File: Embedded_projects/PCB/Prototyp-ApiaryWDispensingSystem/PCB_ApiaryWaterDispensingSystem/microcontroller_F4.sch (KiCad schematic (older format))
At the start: 77 parts, among them J10 Conn_02x19_Odd_Even, J7 Conn_02x19_Odd_Even, SW1 SW_Push_Dual, Y2 Crystal_GND23_Small, Y3 Crystal

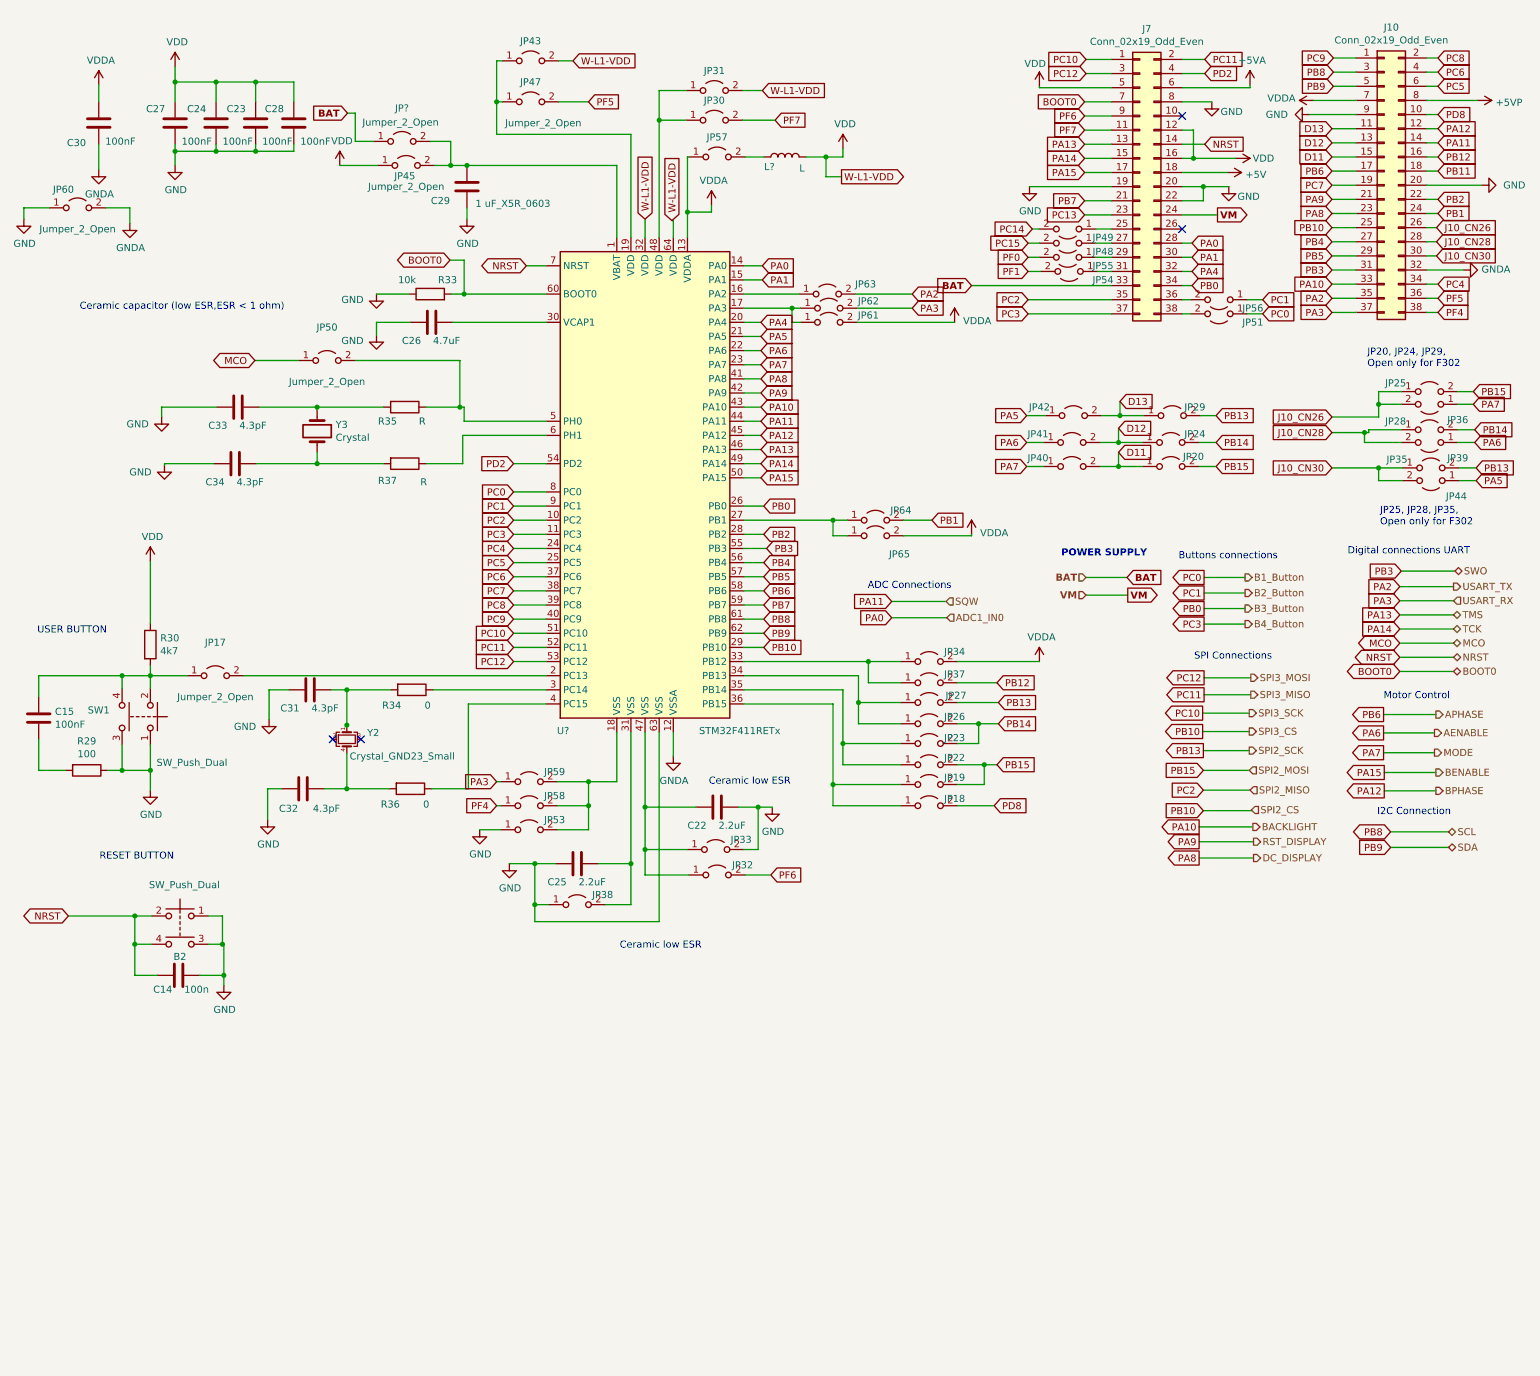
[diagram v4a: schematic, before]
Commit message: All signal has been routed, the analog part needs to be completed
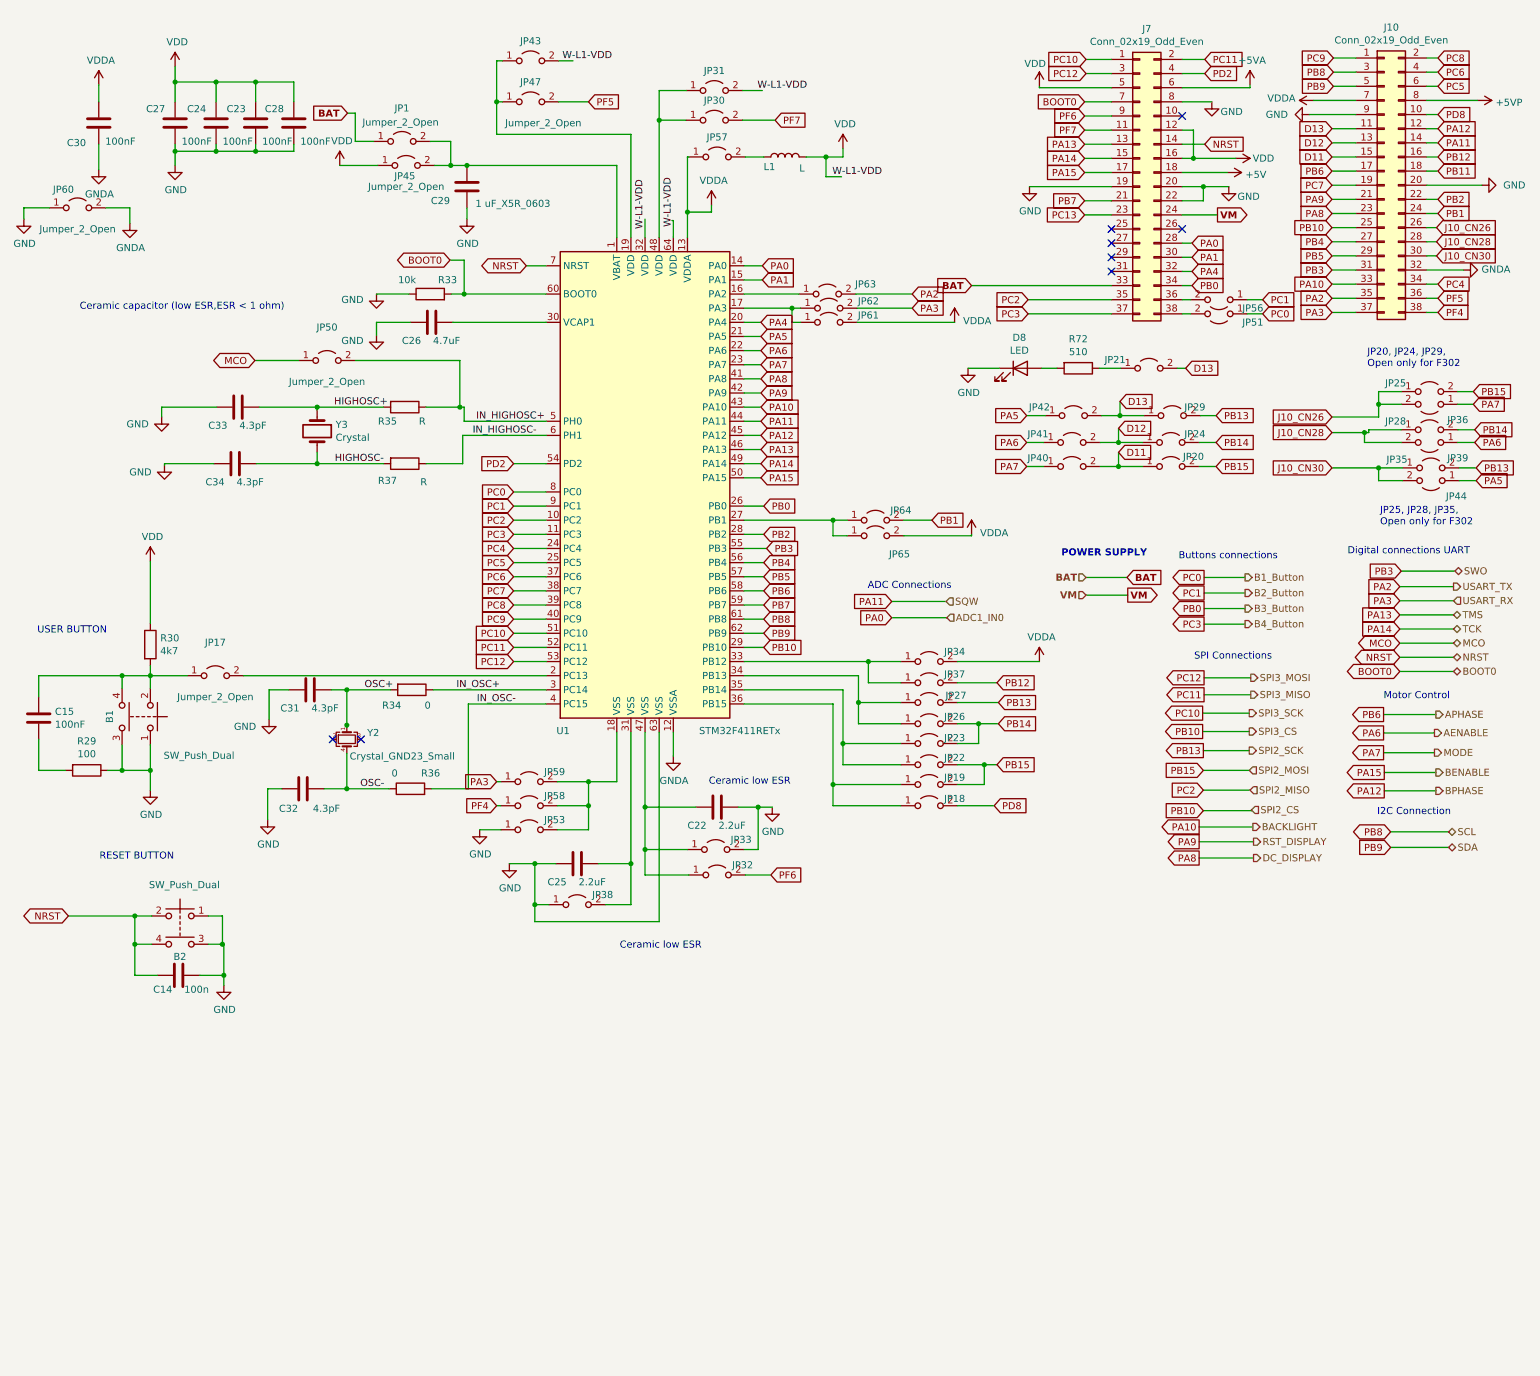
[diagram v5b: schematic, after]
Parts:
- removed JP48, JP49, JP54, JP55: Jumper_2_Open, Jumper:SolderJumper-2_P1.3mm_Open_TrianglePad1.0x1.5mm, symbol Jumper:Jumper_2_Open
- removed SW1: SW_Push_Dual, Button_Switch_SMD:SW_Push_1P1T_NO_6x6mm_H9.5mm, symbol Switch:SW_Push_Dual
- added B1: SW_Push_Dual, Button_Switch_SMD:SW_SPST_Omron_B3FS-100xP, symbol Switch:SW_Push_Dual
- added D8: LED, LED_SMD:LED_0805_2012Metric, symbol Device:LED
- added JP21: Jumper_2_Open, Jumper:SolderJumper-2_P1.3mm_Open_TrianglePad1.0x1.5mm, symbol Jumper:Jumper_2_Open
- added R72: 510, Resistor_SMD:R_0603_1608Metric, symbol Device:R
- B2: footprint Button_Switch_SMD:SW_Push_1P1T_NO_6x6mm_H9.5mm -> Button_Switch_SMD:SW_SPST_Omron_B3FS-100xP
- J10, J7: footprint (none) -> Connector_PinHeader_2.54mm:PinHeader_2x19_P2.54mm_Vertical
- gave numbers to parts that had none: 3
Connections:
- net D13: now also JP21.2 (B)
- net GND: now also B1.1, B1.3, D8.1 (K)
- net at C15.1, JP17.1 (A), R30.2: now also B1.2, B1.4
- net IN_OSC+: now reaches R34.1, U1.3 (PC14)
- net IN_OSC-: now reaches U1.4 (PC15)
- net IN_OSC-: now also R36.2; no longer R36.1
- net IN_HIGHOSC+: now reaches JP50.2 (B), R35.1, U1.5 (PH0)
- net IN_HIGHOSC-: now reaches R37.1, U1.6 (PH1)
- net OSC+: now reaches C31.1, R34.2, Y2.1
- net OSC-: now reaches C32.1, Y2.4
- net OSC-: now also R36.1; no longer R36.2
- net HIGHOSC+: now reaches C33.1, R35.2, Y3.1
- net HIGHOSC-: now reaches C34.1, R37.2, Y3.2
- new net: JP21.1 (A), R72.1
- new net: D8.2 (A), R72.2
- no-connect marks 4 -> 8
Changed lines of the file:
@@
 $EndDescr
-$Comp
-L Switch:SW_Push_Dual SW1
-U 1 1 67E57DF4
-P 1510 5450
-F 0 "SW1" V 1556 5162 50  0000 R CNN
-F 1 "SW_Push_Dual" V 1185 5995 50  0000 R CNN
-F 2 "Button_Switch_SMD:SW_Push_1P1T_NO_6x6mm_H9.5mm" H 1510 5650 50  0001 C CNN
-F 3 "~" H 1510 5650 50  0001 C CNN
-	1    1510 5450
-	0    1    -1   0
-$EndComp
 $Comp
 L Device:R R30
@@
 	1    0    0    -1
 $EndComp
-$Comp
-L MCU_ST_STM32F4:STM32F411RETx U?
-U 1 1 67E5B943
-P 5010 3760
-F 0 "U?" H 4430 1970 50  0000 C CNN
-F 1 "STM32F411RETx" H 5680 1970 50  0000 C CNN
-F 2 "Package_QFP:LQFP-64_10x10mm_P0.5mm" H 4410 2060 50  0001 R CNN
-F 3 "http://www.st.com/st-web-ui/static/active/en/resource/technical/document/datasheet/DM00115249.pdf" H 5010 3760 50  0001 C CNN
-	1    5010 3760
-	1    0    0    -1
-$EndComp
-Wire Wire Line
-	1510 5250 1510 5160
 Wire Wire Line
 	1310 5250 1310 5160
@@
 $EndComp
 Wire Wire Line
-	1510 5650 1510 5830
-Wire Wire Line
 	1310 5650 1310 5830
 Wire Wire Line
 	1310 5830 1510 5830
-Connection ~ 1510 5830
 Wire Wire Line
 	1510 5830 1510 5970
@@
 F 3 "~" H 3350 5960 50  0001 C CNN
 	1    3350 5960
-	0    1    1    0
+	0    -1   -1   0
 $EndComp
 Wire Wire Line
@@
 	3730 3260 3700 3260
 Wire Wire Line
-	3160 3260 2690 3260
-Wire Wire Line
 	2690 3260 2690 3280
 Wire Wire Line
@@
 Wire Wire Line
 	5700 1230 5930 1230
-Text GLabel 4500 810  2    50   Input ~ 0
-W-L1-VDD
-Text GLabel 5010 1930 1    50   Input ~ 0
-W-L1-VDD
 Wire Wire Line
 	4500 810  4400 810
@@
 	5310 1490 5320 1490
 $Comp
-L Device:L L?
+L Device:L L1
 U 1 1 67F1388C
 P 6000 1490
-F 0 "L?" V 5930 1600 50  0000 C CNN
+F 0 "L1" V 5930 1600 50  0000 C CNN
 F 1 "L" V 5920 1370 50  0000 C CNN
 F 2 "Inductor_SMD:L_0603_1608Metric" H 6000 1490 50  0001 C CNN
@@
 	1    0    0    -1
 $EndComp
-Text GLabel 6400 1630 2    50   Output ~ 0
-W-L1-VDD
 Wire Wire Line
 	6150 1490 6290 1490
@@
 Wire Wire Line
 	6510 2660 7200 2660
-Text GLabel 5840 1020 2    50   Input ~ 0
-W-L1-VDD
 Wire Wire Line
 	5840 1020 5700 1020
@@
 F 0 "B2" H 1766 6572 50  0000 R CNN
 F 1 "SW_Push_Dual" H 1940 7080 50  0000 R CNN
-F 2 "Button_Switch_SMD:SW_Push_1P1T_NO_6x6mm_H9.5mm" H 1720 7060 50  0001 C CNN
+F 2 "Button_Switch_SMD:SW_SPST_Omron_B3FS-100xP" H 1720 7060 50  0001 C CNN
 F 3 "~" H 1720 7060 50  0001 C CNN
 	1    1720 6860
@@
 F 0 "J7" H 8560 2817 50  0000 C CNN
 F 1 "Conn_02x19_Odd_Even" H 8560 2726 50  0000 C CNN
-F 2 "" H 8510 1700 50  0001 C CNN
+F 2 "Connector_PinHeader_2.54mm:PinHeader_2x19_P2.54mm_Vertical" H 8510 1700 50  0001 C CNN
 F 3 "~" H 8510 1700 50  0001 C CNN
 	1    8510 1700
@@
 F 0 "J10" H 10290 2807 50  0000 C CNN
 F 1 "Conn_02x19_Odd_Even" H 10290 2716 50  0000 C CNN
-F 2 "" H 10240 1690 50  0001 C CNN
+F 2 "Connector_PinHeader_2.54mm:PinHeader_2x19_P2.54mm_Vertical" H 10240 1690 50  0001 C CNN
 F 3 "~" H 10240 1690 50  0001 C CNN
 	1    10240 1690
@@
 Wire Wire Line
 	8310 1900 8120 1900
-$Comp
-L Jumper:Jumper_2_Open JP49
-U 1 1 684DA5E9
-P 8000 2000
-F 0 "JP49" H 7750 2060 50  0000 C CNN
-F 1 "Jumper_2_Open" H 8090 1850 50  0001 C CNN
-F 2 "Jumper:SolderJumper-2_P1.3mm_Open_TrianglePad1.0x1.5mm" H 8000 2000 50  0001 C CNN
-F 3 "~" H 8000 2000 50  0001 C CNN
-	1    8000 2000
-	-1   0    0    1
-$EndComp
-$Comp
-L Jumper:Jumper_2_Open JP48
-U 1 1 684DACBA
-P 8000 2100
-F 0 "JP48" H 7750 2160 50  0000 C CNN
-F 1 "Jumper_2_Open" H 8090 1950 50  0001 C CNN
-F 2 "Jumper:SolderJumper-2_P1.3mm_Open_TrianglePad1.0x1.5mm" H 8000 2100 50  0001 C CNN
-F 3 "~" H 8000 2100 50  0001 C CNN
-	1    8000 2100
-	-1   0    0    1
-$EndComp
-$Comp
-L Jumper:Jumper_2_Open JP55
-U 1 1 684DAF0A
-P 8000 2200
-F 0 "JP55" H 7750 2260 50  0000 C CNN
-F 1 "Jumper_2_Open" H 8090 2050 50  0001 C CNN
-F 2 "Jumper:SolderJumper-2_P1.3mm_Open_TrianglePad1.0x1.5mm" H 8000 2200 50  0001 C CNN
-F 3 "~" H 8000 2200 50  0001 C CNN
-	1    8000 2200
-	-1   0    0    1
-$EndComp
-$Comp
-L Jumper:Jumper_2_Open JP54
-U 1 1 684DB210
-P 8010 2300
-F 0 "JP54" H 7770 2360 50  0000 C CNN
-F 1 "Jumper_2_Open" H 8100 2150 50  0001 C CNN
-F 2 "Jumper:SolderJumper-2_P1.3mm_Open_TrianglePad1.0x1.5mm" H 8010 2300 50  0001 C CNN
-F 3 "~" H 8010 2300 50  0001 C CNN
-	1    8010 2300
-	-1   0    0    1
-$EndComp
-Text GLabel 7750 2000 0    50   Input ~ 0
-PC14
-Text GLabel 7720 2100 0    50   Input ~ 0
-PC15
-Text GLabel 7720 2200 0    50   Input ~ 0
-PF0
-Text GLabel 7720 2300 0    50   Input ~ 0
-PF1
-Wire Wire Line
-	7800 2000 7750 2000
-Wire Wire Line
-	7720 2100 7800 2100
-Wire Wire Line
-	7720 2200 7800 2200
-Wire Wire Line
-	8310 2000 8200 2000
-Wire Wire Line
-	8200 2100 8310 2100
-Wire Wire Line
-	8310 2200 8200 2200
-Wire Wire Line
-	8210 2300 8310 2300
-Wire Wire Line
-	7720 2300 7810 2300
 Text GLabel 7720 2500 0    50   Input ~ 0
 PC2
@@
 Wire Wire Line
 	7320 2400 8310 2400
-Text GLabel 5200 1940 1    50   Input ~ 0
-W-L1-VDD
 Wire Wire Line
 	3750 1550 3635 1550
@@
 	8960 6115 9300 6115
 $Comp
-L Jumper:Jumper_2_Open JP?
+L Jumper:Jumper_2_Open JP1
 U 1 1 68F03CE2
 P 3290 1380
-F 0 "JP?" H 3290 1615 50  0000 C CNN
+F 0 "JP1" H 3290 1615 50  0000 C CNN
 F 1 "Jumper_2_Open" H 3280 1515 50  0000 C CNN
 F 2 "Jumper:SolderJumper-2_P1.3mm_Open_TrianglePad1.0x1.5mm" H 3290 1380 50  0001 C CNN
@@
 Wire Wire Line
 	8930 6450 9315 6450
+$Comp
+L Switch:SW_Push_Dual B1
+U 1 1 690C2C64
+P 1510 5450
+F 0 "B1" H 1556 5162 50  0000 R CNN
+F 1 "SW_Push_Dual" V 1235 6045 50  0000 R CNN
+F 2 "Button_Switch_SMD:SW_SPST_Omron_B3FS-100xP" H 1510 5650 50  0001 C CNN
+F 3 "~" H 1510 5650 50  0001 C CNN
+	1    1510 5450
+	0    1    -1   0
+$EndComp
+Wire Wire Line
+	1510 5250 1510 5160
+Wire Wire Line
+	1510 5160 1510 5155
+Wire Wire Line
+	1510 5650 1510 5830
+Connection ~ 1510 5830
+Text GLabel 8835 2985 2    50   Input ~ 0
+D13
+$Comp
+L Device:R R72
+U 1 1 68FB6AB0
+P 8075 2985
+F 0 "R72" V 7868 2985 50  0000 C CNN
+F 1 "510" V 7959 2985 50  0000 C CNN
+F 2 "Resistor_SMD:R_0603_1608Metric" V 8005 2985 50  0001 C CNN
+F 3 "~" H 8075 2985 50  0001 C CNN
+	1    8075 2985
+	0    1    1    0
+$EndComp
+$Comp
+L power:GND #PWR038
+U 1 1 68FE9C57
+P 7295 2985
+F 0 "#PWR038" H 7295 2735 50  0001 C CNN
+F 1 "GND" H 7300 2812 50  0000 C CNN
+F 2 "" H 7295 2985 50  0001 C CNN
+F 3 "" H 7295 2985 50  0001 C CNN
+	1    7295 2985
+	1    0    0    -1
+$EndComp
+Wire Wire Line
+	7295 2985 7515 2985
+Wire Wire Line
+	7815 2985 7925 2985
+Wire Wire Line
+	8375 2985 8225 2985
+$Comp
+L Jumper:Jumper_2_Open JP21
+U 1 1 69080A2B
+P 8575 2985
+F 0 "JP21" H 8335 3045 50  0000 C CNN
+F 1 "Jumper_2_Open" H 8665 2835 50  0001 C CNN
+F 2 "Jumper:SolderJumper-2_P1.3mm_Open_TrianglePad1.0x1.5mm" H 8575 2985 50  0001 C CNN
+F 3 "~" H 8575 2985 50  0001 C CNN
+	1    8575 2985
+	1    0    0    -1
+$EndComp
+Wire Wire Line
+	8835 2985 8775 2985
+$Comp
+L Device:LED D8
+U 1 1 68FB841B
+P 7665 2985
+F 0 "D8" H 7658 3202 50  0000 C CNN
+F 1 "LED" H 7658 3111 50  0000 C CNN
+F 2 "LED_SMD:LED_0805_2012Metric" H 7665 2985 50  0001 C CNN
+F 3 "~" H 7665 2985 50  0001 C CNN
+	1    7665 2985
+	1    0    0    -1
+$EndComp
+Text Label 5210 1985 1    50   ~ 0
+W-L1-VDD
+Text Label 5010 2000 1    50   ~ 0
+W-L1-VDD
+Text Label 6335 1630 0    50   ~ 0
+W-L1-VDD
+Text Label 4425 810  0    50   ~ 0
+W-L1-VDD
+Text Label 5805 1020 0    50   ~ 0
+W-L1-VDD
+Wire Wire Line
+	3160 3260 2690 3260
+Text Label 2995 5960 0    50   ~ 0
+OSC-
+Text Label 3025 5260 0    50   ~ 0
+OSC+
+Text Label 2810 3260 0    50   ~ 0
+HIGHOSC+
+Text Label 2815 3660 0    50   ~ 0
+HIGHOSC-
+Text Label 3675 5260 0    50   ~ 0
+IN_OSC+
+Text Label 3820 5360 0    50   ~ 0
+IN_OSC-
+Text Label 3815 3360 0    50   ~ 0
+IN_HIGHOSC+
+Text Label 3790 3460 0    50   ~ 0
+IN_HIGHOSC-
+NoConn ~ 8310 2000
+NoConn ~ 8310 2100
+NoConn ~ 8310 2200
+NoConn ~ 8310 2300
+$Comp
+L MCU_ST_STM32F4:STM32F411RETx U1
+U 1 1 67E5B943
+P 5010 3760
+F 0 "U1" H 4430 1970 50  0000 C CNN
+F 1 "STM32F411RETx" H 5680 1970 50  0000 C CNN
+F 2 "Package_QFP:LQFP-64_10x10mm_P0.5mm" H 4410 2060 50  0001 R CNN
+F 3 "http://www.st.com/st-web-ui/static/active/en/resource/technical/document/datasheet/DM00115249.pdf" H 5010 3760 50  0001 C CNN
+	1    5010 3760
+	1    0    0    -1
+$EndComp
 $EndSCHEMATC
